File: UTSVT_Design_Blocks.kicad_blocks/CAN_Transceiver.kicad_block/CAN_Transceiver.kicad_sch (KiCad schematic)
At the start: 7 parts, among them IC1 TCAN3413DR

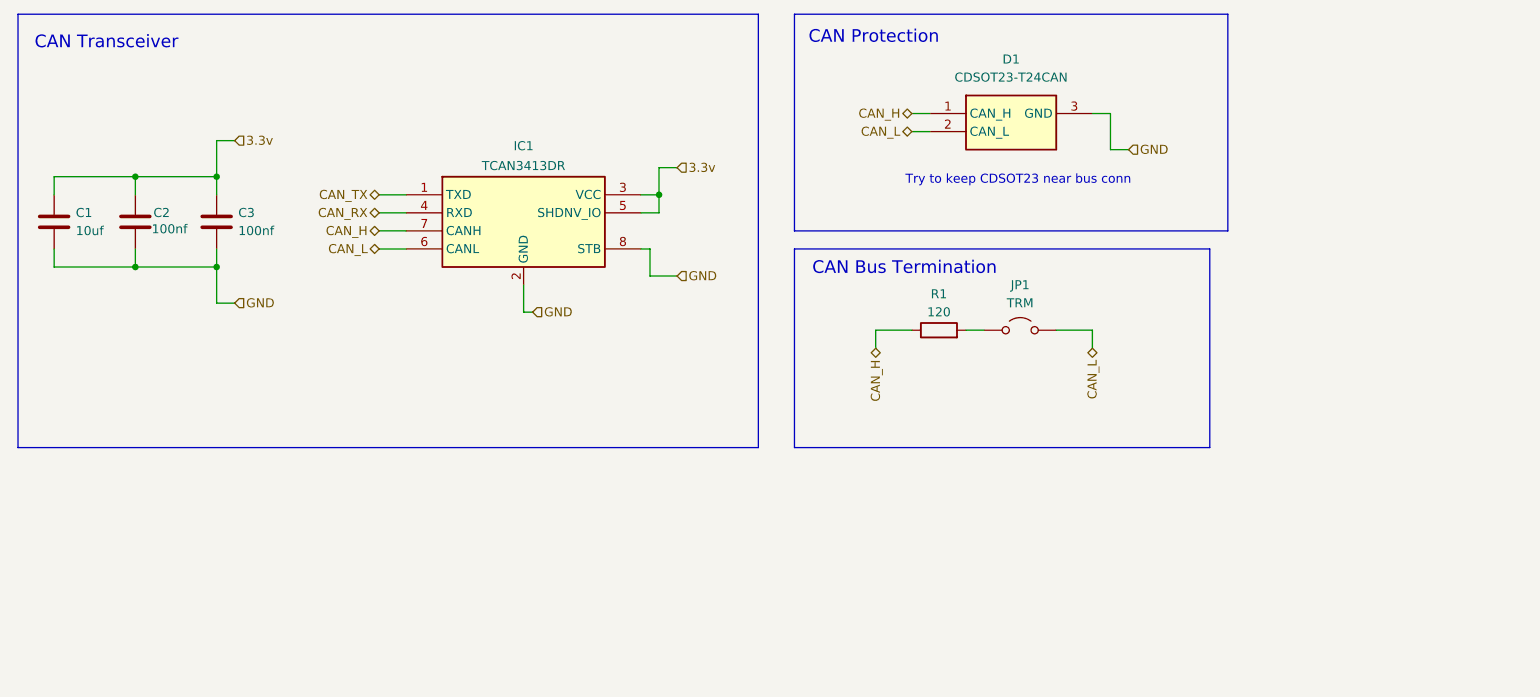
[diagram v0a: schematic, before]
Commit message: switched to split termination + hopefully fixed symbols
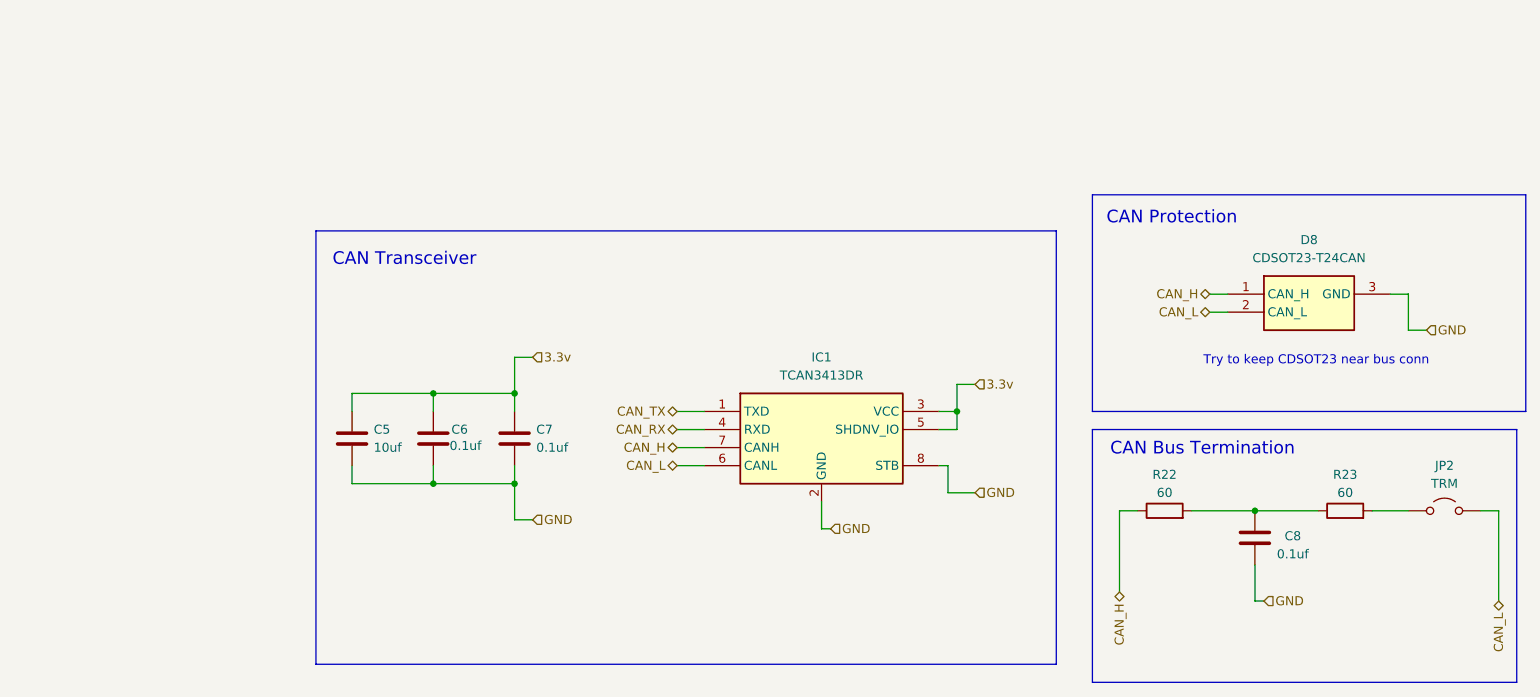
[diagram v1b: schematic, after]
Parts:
- removed D1: CDSOT23-T24CAN, UTSVT_CANTRANSIEVER:SOT95P230X117-3N, symbol CDSOT23-T24CAN:CDSOT23-T24CAN
- added C8: 0.1uf, ECE319K:C_Axial_200mil, symbol ECE319K:C
- added D8: CDSOT23-T24CAN, SOT95P230X117-3N, symbol CDSOT23-T24CAN:CDSOT23-T24CAN
- added R23: 60, Resistor_SMD:R_0603_1608Metric_Pad0.98x0.95mm_HandSolder, symbol Device:R
- C6: renamed from C2; value 100nf -> 0.1uf
- C7: renamed from C3; value 100nf -> 0.1uf
- IC1: footprint UTSVT_CANTRANSIEVER:SOIC127P600X175-8N -> SOIC127P600X175-8N; LCSC P/N (none) -> C22433320; Manufacturer_Part_Number TCAN3413DR -> (none); Mouser Price/Stock https://www.mouser.co.uk/ProductDetail/Texas-Instruments/TC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 -> -; P/N (none) -> TCAN3413DR
- R22: renamed from R1; value 120 -> 60
- renumbered C1 to C5, JP1 to JP2
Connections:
- net CAN_H: now also D8.1 (CAN_H)
- net CAN_L: now also D8.2 (CAN_L)
- net GND: now also C8.1, D8.3 (GND)
- net at R22.2: now also C8.2, R23.1; no longer JP2.1 (A)
- new net: JP2.1 (A), R23.2
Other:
- moved on the sheet: C5, C6, C7, JP2, R22

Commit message: fixed issues
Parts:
- C1: renamed from C5; value 10uf -> 10u; LCSC P/N (none) -> C440198; P/N (none) -> GRM21BR61H106KE43K
- C2: renamed from C6; value 0.1uf -> 0.1u; LCSC P/N (none) -> C14663; P/N (none) -> MLASH168SB7104KTNA01
- C3: renamed from C7; value 0.1uf -> 0.1u; LCSC P/N (none) -> C14663; P/N (none) -> MLASH168SB7104KTNA01
- C4: renamed from C8; value 0.1uf -> 0.1u; footprint ECE319K:C_Axial_200mil -> Capacitor_SMD:C_0603_1608Metric_Pad1.08x0.95mm_HandSolder; LCSC P/N (none) -> C14663; P/N (none) -> MLASH168SB7104KTNA01
- D1: renamed from D8; footprint SOT95P230X117-3N -> UTSVT_Passives:SOT95P230X117-3N
- IC1: footprint SOIC127P600X175-8N -> UTSVT_Passives:SOIC127P600X175-8N
- R1: renamed from R22; LCSC P/N (none) -> C166918; P/N (none) -> RTT0360R0FTP
- R2: renamed from R23; LCSC P/N (none) -> C166918; P/N (none) -> RTT0360R0FTP
- renumbered JP2 to JP1
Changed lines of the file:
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@@
 		(on_board yes)
 		(dnp no)
-		(property "Reference" "C6"
+		(property "Reference" "C2"
 			(at 76.2 73.66 0)
 			(effects
@@
 			)
 		)
-		(property "Value" "0.1uf"
+		(property "Value" "0.1u"
 			(at 75.946 75.946 0)
 			(effects
@@
 			)
 		)
+		(property "LCSC P/N" "C14663"
+			(at 73.66 74.93 0)
+			(effects
+				(font
+					(size 1.27 1.27)
+				)
+				(hide yes)
+			)
+		)
+		(property "P/N" "MLASH168SB7104KTNA01"
+			(at 73.66 74.93 0)
+			(effects
+				(font
+					(size 1.27 1.27)
+				)
+				(hide yes)
+			)
+		)
 		(pin "1"
 		)
@@
 			)
 			(project "CAN_Transceiver"
-				(path "/81d906df-a099-480a-8398-28a8e913d125"
+				(path "/a09f9696-80ee-4697-8aaa-225f287b667b"
 					(reference "C2")
 					(unit 1)
@@
 		(on_board yes)
 		(dnp no)
-		(property "Reference" "C8"
+		(property "Reference" "C4"
 			(at 194.564 88.646 0)
 			(effects
@@
 			)
 		)
-		(property "Value" "0.1uf"
+		(property "Value" "0.1u"
 			(at 194.564 91.186 0)
 			(effects
@@
 			)
 		)
-		(property "Footprint" "ECE319K:C_Axial_200mil"
+		(property "Footprint" "Capacitor_SMD:C_0603_1608Metric_Pad1.08x0.95mm_HandSolder"
 			(at 188.2648 85.09 0)
 			(effects
@@
 			)
 		)
+		(property "LCSC P/N" "C14663"
+			(at 189.23 88.9 0)
+			(effects
+				(font
+					(size 1.27 1.27)
+				)
+				(hide yes)
+			)
+		)
+		(property "P/N" "MLASH168SB7104KTNA01"
+			(at 189.23 88.9 0)
+			(effects
+				(font
+					(size 1.27 1.27)
+				)
+				(hide yes)
+			)
+		)
 		(pin "1"
 		)
@@
 				(path "/69b823fd-c065-40ff-9bb9-c5835555f3eb/9d9eae1e-c713-4323-9845-a569cff8d5d3"
 					(reference "C8")
+					(unit 1)
+				)
+			)
+			(project "CAN_Transceiver"
+				(path "/a09f9696-80ee-4697-8aaa-225f287b667b"
+					(reference "C4")
 					(unit 1)
 				)
@@
 		(dnp no)
 		(fields_autoplaced yes)
-		(property "Reference" "JP2"
+		(property "Reference" "JP1"
 			(at 215.9 78.74 0)
 			(effects
@@
 			(project ""
 				(path "/81d906df-a099-480a-8398-28a8e913d125"
+					(reference "JP1")
+					(unit 1)
+				)
+			)
+			(project "CAN_Transceiver"
+				(path "/a09f9696-80ee-4697-8aaa-225f287b667b"
 					(reference "JP1")
 					(unit 1)
@@
 		(on_board yes)
 		(dnp no)
-		(property "Reference" "C7"
+		(property "Reference" "C3"
 			(at 88.138 73.66 0)
 			(effects
@@
 			)
 		)
-		(property "Value" "0.1uf"
+		(property "Value" "0.1u"
 			(at 88.138 76.2 0)
 			(effects
@@
 			)
 		)
+		(property "LCSC P/N" "C14663"
+			(at 85.09 74.93 0)
+			(effects
+				(font
+					(size 1.27 1.27)
+				)
+				(hide yes)
+			)
+		)
+		(property "P/N" "MLASH168SB7104KTNA01"
+			(at 85.09 74.93 0)
+			(effects
+				(font
+					(size 1.27 1.27)
+				)
+				(hide yes)
+			)
+		)
 		(pin "1"
 		)
@@
 			)
 			(project "CAN_Transceiver"
-				(path "/81d906df-a099-480a-8398-28a8e913d125"
+				(path "/a09f9696-80ee-4697-8aaa-225f287b667b"
 					(reference "C3")
 					(unit 1)
@@
 		(on_board yes)
 		(dnp no)
-		(property "Reference" "C5"
+		(property "Reference" "C1"
 			(at 65.278 73.66 0)
 			(effects
@@
 			)
 		)
-		(property "Value" "10uf"
+		(property "Value" "10u"
 			(at 65.278 76.2 0)
 			(effects
@@
 			)
 		)
+		(property "LCSC P/N" "C440198"
+			(at 62.23 74.93 0)
+			(effects
+				(font
+					(size 1.27 1.27)
+				)
+				(hide yes)
+			)
+		)
+		(property "P/N" "GRM21BR61H106KE43K"
+			(at 62.23 74.93 0)
+			(effects
+				(font
+					(size 1.27 1.27)
+				)
+				(hide yes)
+			)
+		)
 		(pin "1"
 		)
@@
 			(project ""
 				(path "/81d906df-a099-480a-8398-28a8e913d125"
+					(reference "C1")
+					(unit 1)
+				)
+			)
+			(project "CAN_Transceiver"
+				(path "/a09f9696-80ee-4697-8aaa-225f287b667b"
 					(reference "C1")
 					(unit 1)
@@
 		(on_board yes)
 		(dnp no)
-		(property "Reference" "R23"
+		(property "Reference" "R2"
 			(at 201.93 80.01 90)
 			(effects
@@
 		(property "Description" "Resistor"
 			(at 201.93 85.09 0)
+			(effects
+				(font
+					(size 1.27 1.27)
+				)
+				(hide yes)
+			)
+		)
+		(property "LCSC P/N" "C166918"
+			(at 201.93 85.09 90)
+			(effects
+				(font
+					(size 1.27 1.27)
+				)
+				(hide yes)
+			)
+		)
+		(property "P/N" "RTT0360R0FTP"
+			(at 201.93 85.09 90)
 			(effects
 				(font
@@
 				(path "/69b823fd-c065-40ff-9bb9-c5835555f3eb/9d9eae1e-c713-4323-9845-a569cff8d5d3"
 					(reference "R23")
+					(unit 1)
+				)
+			)
+			(project "CAN_Transceiver"
+				(path "/a09f9696-80ee-4697-8aaa-225f287b667b"
+					(reference "R2")
 					(unit 1)
 				)
@@
 		(dnp no)
 		(fields_autoplaced yes)
-		(property "Reference" "D8"
+		(property "Reference" "D1"
 			(at 196.85 46.99 0)
 			(effects
@@
 			)
 		)
-		(property "Footprint" "SOT95P230X117-3N"
+		(property "Footprint" "UTSVT_Passives:SOT95P230X117-3N"
 			(at 204.47 149.53 0)
 			(effects
@@
 				(path "/69b823fd-c065-40ff-9bb9-c5835555f3eb/9d9eae1e-c713-4323-9845-a569cff8d5d3"
 					(reference "D8")
+					(unit 1)
+				)
+			)
+			(project "CAN_Transceiver"
+				(path "/a09f9696-80ee-4697-8aaa-225f287b667b"
+					(reference "D1")
 					(unit 1)
 				)
@@
 			)
 		)
-		(property "Footprint" "SOIC127P600X175-8N"
+		(property "Footprint" "UTSVT_Passives:SOIC127P600X175-8N"
 			(at 140.97 166.04 0)
 			(effects
@@
 			(project ""
 				(path "/69b823fd-c065-40ff-9bb9-c5835555f3eb/9d9eae1e-c713-4323-9845-a569cff8d5d3"
+					(reference "IC1")
+					(unit 1)
+				)
+			)
+			(project "CAN_Transceiver"
+				(path "/a09f9696-80ee-4697-8aaa-225f287b667b"
 					(reference "IC1")
 					(unit 1)
@@
 		(on_board yes)
 		(dnp no)
-		(property "Reference" "R22"
+		(property "Reference" "R1"
 			(at 176.53 80.01 90)
 			(effects
@@
 			)
 		)
+		(property "LCSC P/N" "C166918"
+			(at 176.53 85.09 90)
+			(effects
+				(font
+					(size 1.27 1.27)
+				)
+				(hide yes)
+			)
+		)
+		(property "P/N" "RTT0360R0FTP"
+			(at 176.53 85.09 90)
+			(effects
+				(font
+					(size 1.27 1.27)
+				)
+				(hide yes)
+			)
+		)
 		(pin "1"
 		)
@@
 				)
 			)
+			(project "CAN_Transceiver"
+				(path "/a09f9696-80ee-4697-8aaa-225f287b667b"
+					(reference "R1")
+					(unit 1)
+				)
+			)
 		)
 	)
+	(sheet_instances
+		(path "/"
+			(page "1")
+		)
+	)
+	(embedded_fonts no)
 )

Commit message: hopefully fixed footprints + parts
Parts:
- D1: footprint UTSVT_Passives:SOT95P230X117-3N -> UTSVT_Passives:CDSOT23-T24CAN
- IC1: footprint UTSVT_Passives:SOIC127P600X175-8N -> UTSVT_Passives:TCAN3413DR
- R1, R2: P/N RTT0360R0FTP -> CRCW060360R4FKEA
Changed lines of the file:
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@@
 	)
 	(hierarchical_label "CAN_TX"
-		(shape bidirectional)
+		(shape input)
 		(at 107.95 71.12 180)
 		(effects
@@
 	)
 	(hierarchical_label "CAN_RX"
-		(shape bidirectional)
+		(shape output)
 		(at 107.95 73.66 180)
 		(effects
@@
 			)
 		)
-		(property "P/N" "RTT0360R0FTP"
+		(property "P/N" "CRCW060360R4FKEA"
 			(at 201.93 85.09 90)
 			(effects
@@
 			)
 		)
-		(property "Footprint" "UTSVT_Passives:SOT95P230X117-3N"
+		(property "Footprint" "UTSVT_Passives:CDSOT23-T24CAN"
 			(at 204.47 149.53 0)
 			(effects
@@
 			)
 		)
-		(property "Footprint" "UTSVT_Passives:SOIC127P600X175-8N"
+		(property "Footprint" "UTSVT_Passives:TCAN3413DR"
 			(at 140.97 166.04 0)
 			(effects
@@
 			)
 		)
-		(property "P/N" "RTT0360R0FTP"
+		(property "P/N" "CRCW060360R4FKEA"
 			(at 176.53 85.09 90)
 			(effects
